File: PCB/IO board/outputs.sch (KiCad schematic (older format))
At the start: 20 parts

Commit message: Schematics Rev 1.0
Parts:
- gave numbers to parts that had none: 17
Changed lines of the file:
@@
 $Descr A4 11693 8268
 encoding utf-8
-Sheet 3 7
+Sheet 3 8
 Title ""
 Date ""
@@
 $EndDescr
 $Comp
-L MCP6004 U?
+L MCP6004 U301
 U 1 1 5ADC7D64
 P 2550 1700
-F 0 "U?" H 2550 1900 50  0000 L CNN
+F 0 "U301" H 2550 1900 50  0000 L CNN
 F 1 "TLV9064" H 2550 1500 50  0000 L CNN
 F 2 "" H 2500 1800 50  0001 C CNN
@@
 $EndComp
 $Comp
-L MCP6004 U?
+L MCP6004 U301
 U 2 1 5ADC7E6B
 P 2550 2600
-F 0 "U?" H 2550 2800 50  0000 L CNN
+F 0 "U301" H 2550 2800 50  0000 L CNN
 F 1 "TLV9064" H 2550 2400 50  0000 L CNN
 F 2 "" H 2500 2700 50  0001 C CNN
@@
 $EndComp
 $Comp
-L MCP6004 U?
+L MCP6004 U301
 U 3 1 5ADC7FEE
 P 2250 5000
-F 0 "U?" H 2250 5200 50  0000 L CNN
+F 0 "U301" H 2250 5200 50  0000 L CNN
 F 1 "TLV9064" H 2250 4800 50  0000 L CNN
 F 2 "" H 2200 5100 50  0001 C CNN
@@
 $EndComp
 $Comp
-L MCP6004 U?
+L MCP6004 U301
 U 4 1 5ADC8017
 P 2250 5900
-F 0 "U?" H 2250 6100 50  0000 L CNN
+F 0 "U301" H 2250 6100 50  0000 L CNN
 F 1 "TLV9064" H 2250 5700 50  0000 L CNN
 F 2 "" H 2200 6000 50  0001 C CNN
@@
 $EndComp
 $Comp
-L R R?
+L R R301
 U 1 1 5ADC8278
 P 1675 1600
-F 0 "R?" V 1755 1600 50  0000 C CNN
+F 0 "R301" V 1755 1600 50  0000 C CNN
 F 1 "51R" V 1675 1600 50  0000 C CNN
 F 2 "" V 1605 1600 50  0001 C CNN
@@
 $EndComp
 $Comp
-L C_Small C?
+L C_Small C302
 U 1 1 5ADC8327
 P 1925 2150
-F 0 "C?" H 1935 2220 50  0000 L CNN
+F 0 "C302" H 1935 2220 50  0000 L CNN
 F 1 "68nF" H 1935 2070 50  0000 L CNN
 F 2 "" H 1925 2150 50  0001 C CNN
@@
 $EndComp
 $Comp
-L GND #PWR?
+L GND #PWR016
 U 1 1 5ADC8546
 P 2400 2000
-F 0 "#PWR?" H 2400 1750 50  0001 C CNN
+F 0 "#PWR016" H 2400 1750 50  0001 C CNN
 F 1 "GND" H 2400 1850 50  0000 C CNN
 F 2 "" H 2400 2000 50  0001 C CNN
@@
 	2150 1800 2250 1800
 $Comp
-L GND #PWR?
+L GND #PWR017
 U 1 1 5ADC86E7
 P 2400 2300
-F 0 "#PWR?" H 2400 2050 50  0001 C CNN
+F 0 "#PWR017" H 2400 2050 50  0001 C CNN
 F 1 "GND" H 2400 2150 50  0000 C CNN
 F 2 "" H 2400 2300 50  0001 C CNN
@@
 	1825 2700 2250 2700
 $Comp
-L R R?
+L R R302
 U 1 1 5ADC8ADD
 P 1675 2700
-F 0 "R?" V 1755 2700 50  0000 C CNN
+F 0 "R302" V 1755 2700 50  0000 C CNN
 F 1 "51R" V 1675 2700 50  0000 C CNN
 F 2 "" V 1605 2700 50  0001 C CNN
@@
 	2450 2900 2450 3100
 $Comp
-L C_Small C?
+L C_Small C303
 U 1 1 5ADC9661
 P 3500 2600
-F 0 "C?" V 3550 2675 50  0000 L CNN
+F 0 "C303" V 3550 2675 50  0000 L CNN
 F 1 "10uF 100V" V 3550 2150 50  0000 L CNN
 F 2 "" H 3500 2600 50  0001 C CNN
@@
 $EndComp
 $Comp
-L D_Schottky_x2_ACom_KKA D?
+L D_Schottky_x2_ACom_KKA D301
 U 1 1 5ADC9B8C
 P 3125 2150
-F 0 "D?" V 3250 2000 50  0000 C CNN
+F 0 "D301" V 3250 2000 50  0000 C CNN
 F 1 "MMBZ5V6ALT1G" V 3025 1750 50  0000 C CNN
 F 2 "" H 3125 2150 50  0001 C CNN
@@
 Connection ~ 2950 2600
 $Comp
-L C_Small C?
+L C_Small C301
 U 1 1 5ADCA264
 P 3500 1700
-F 0 "C?" V 3550 1775 50  0000 L CNN
+F 0 "C301" V 3550 1775 50  0000 L CNN
 F 1 "10uF 100V" V 3550 1250 50  0000 L CNN
 F 2 "" H 3500 1700 50  0001 C CNN
@@
 $EndComp
 $Comp
-L Audio-Jack-3 J?
+L Audio-Jack-3 J301
 U 1 1 5ADCA5E0
 P 4300 2100
-F 0 "J?" H 4375 2025 50  0000 C CNN
+F 0 "J301" H 4375 2025 50  0000 C CNN
 F 1 "Audio-Jack-3" H 4150 2275 50  0000 C CNN
 F 2 "" H 4550 2200 50  0001 C CNN
@@
 	4500 1900 4600 1900
 $Comp
-L GND #PWR?
+L GND #PWR018
 U 1 1 5ADCB98E
 P 2100 5300
-F 0 "#PWR?" H 2100 5050 50  0001 C CNN
+F 0 "#PWR018" H 2100 5050 50  0001 C CNN
 F 1 "GND" H 2100 5150 50  0000 C CNN
 F 2 "" H 2100 5300 50  0001 C CNN
@@
 $EndComp
 $Comp
-L GND #PWR?
+L GND #PWR019
 U 1 1 5ADCB9D7
 P 2100 5600
-F 0 "#PWR?" H 2100 5350 50  0001 C CNN
+F 0 "#PWR019" H 2100 5350 50  0001 C CNN
 F 1 "GND" H 2100 5450 50  0000 C CNN
 F 2 "" H 2100 5600 50  0001 C CNN
@@
 	2150 4600 2150 4700
 $Comp
-L C_Small C?
+L C_Small C304
 U 1 1 5ADCC56F
 P 2450 3200
-F 0 "C?" H 2460 3270 50  0000 L CNN
+F 0 "C304" H 2460 3270 50  0000 L CNN
 F 1 "100nF" H 2460 3120 50  0000 L CNN
 F 2 "" H 2450 3200 50  0001 C CNN
@@
 Connection ~ 2450 3000
 $Comp
-L GND #PWR?
+L GND #PWR020
 U 1 1 5ADCC68B
 P 2450 3400
-F 0 "#PWR?" H 2450 3150 50  0001 C CNN
+F 0 "#PWR020" H 2450 3150 50  0001 C CNN
 F 1 "GND" H 2450 3250 50  0000 C CNN
 F 2 "" H 2450 3400 50  0001 C CNN
@@
 	2450 3300 2450 3400
 $Comp
-L C_Small C?
+L C_Small C306
 U 1 1 5ADCD4D6
 P 1625 5100
-F 0 "C?" H 1635 5170 50  0000 L CNN
+F 0 "C306" H 1635 5170 50  0000 L CNN
 F 1 "68nF" H 1635 5020 50  0000 L CNN
 F 2 "" H 1625 5100 50  0001 C CNN
@@
 	1525 4900 1950 4900
 $Comp
-L C_Small C?
+L C_Small C307
 U 1 1 5ADCD905
 P 1625 5800
-F 0 "C?" H 1635 5870 50  0000 L CNN
+F 0 "C307" H 1635 5870 50  0000 L CNN
 F 1 "68nF" H 1635 5720 50  0000 L CNN
 F 2 "" H 1625 5800 50  0001 C CNN
@@
 	1625 6000 1625 5900
 $Comp
-L GND #PWR?
+L GND #PWR021
 U 1 1 5ADCDA87
 P 1625 5250
-F 0 "#PWR?" H 1625 5000 50  0001 C CNN
+F 0 "#PWR021" H 1625 5000 50  0001 C CNN
 F 1 "GND" H 1625 5100 50  0000 C CNN
 F 2 "" H 1625 5250 50  0001 C CNN
@@
 $EndComp
 $Comp
-L GND #PWR?
+L GND #PWR022
 U 1 1 5ADCDAC2
 P 1625 5650
-F 0 "#PWR?" H 1625 5400 50  0001 C CNN
+F 0 "#PWR022" H 1625 5400 50  0001 C CNN
 F 1 "GND" H 1625 5500 50  0000 C CNN
 F 2 "" H 1625 5650 50  0001 C CNN
@@
 	1625 5700 1625 5650
 $Comp
-L R R?
+L R R303
 U 1 1 5ADCDD04
 P 1375 4900
-F 0 "R?" V 1455 4900 50  0000 C CNN
+F 0 "R303" V 1455 4900 50  0000 C CNN
 F 1 "100R" V 1375 4900 50  0000 C CNN
 F 2 "" V 1305 4900 50  0001 C CNN
@@
 $EndComp
 $Comp
-L R R?
+L R R304
 U 1 1 5ADCDFDD
 P 1375 6000
-F 0 "R?" V 1455 6000 50  0000 C CNN
+F 0 "R304" V 1455 6000 50  0000 C CNN
 F 1 "100R" V 1375 6000 50  0000 C CNN
 F 2 "" V 1305 6000 50  0001 C CNN
@@
 	1125 4900 1225 4900
 $Comp
-L D_Schottky_x2_ACom_KKA D?
+L D_Schottky_x2_ACom_KKA D302
 U 1 1 5ADCF378
 P 2850 5450
-F 0 "D?" V 2975 5300 50  0000 C CNN
+F 0 "D302" V 2975 5300 50  0000 C CNN
 F 1 "MMBZ5V6ALT1G" V 2750 5050 50  0000 C CNN
 F 2 "" H 2850 5450 50  0001 C CNN
@@
 Connection ~ 2650 5900
 $Comp
-L GND #PWR?
+L GND #PWR023
 U 1 1 5ADCF790
 P 3150 5450
-F 0 "#PWR?" H 3150 5200 50  0001 C CNN
+F 0 "#PWR023" H 3150 5200 50  0001 C CNN
 F 1 "GND" V 3200 5275 50  0000 C CNN
 F 2 "" H 3150 5450 50  0001 C CNN
@@
 	3050 5450 3150 5450
 $Comp
-L C_Small C?
+L C_Small C305
 U 1 1 5ADCF9BE
 P 3050 5000
-F 0 "C?" V 3100 5075 50  0000 L CNN
+F 0 "C305" V 3100 5075 50  0000 L CNN
 F 1 "10uF 10V" V 3100 4550 50  0000 L CNN
 F 2 "" H 3050 5000 50  0001 C CNN
@@
 $EndComp
 $Comp
-L C_Small C?
+L C_Small C308
 U 1 1 5ADCFBDE
 P 3050 5900
-F 0 "C?" V 3100 5975 50  0000 L CNN
+F 0 "C308" V 3100 5975 50  0000 L CNN
 F 1 "10uF 10V" V 3100 5450 50  0000 L CNN
 F 2 "" H 3050 5900 50  0001 C CNN
@@
 Connection ~ 2850 5000
 $Comp
-L 3.5mm_TRS_2SW X?
+L 3.5mm_TRS_2SW X301
 U 1 1 5ADD0316
 P 4175 5450
-F 0 "X?" H 4175 5800 60  0000 C CNN
+F 0 "X301" H 4175 5800 60  0000 C CNN
 F 1 "3.5mm_TRS_2SW" H 4575 5100 60  0000 C CNN
 F 2 "" H 3975 5450 60  0001 C CNN

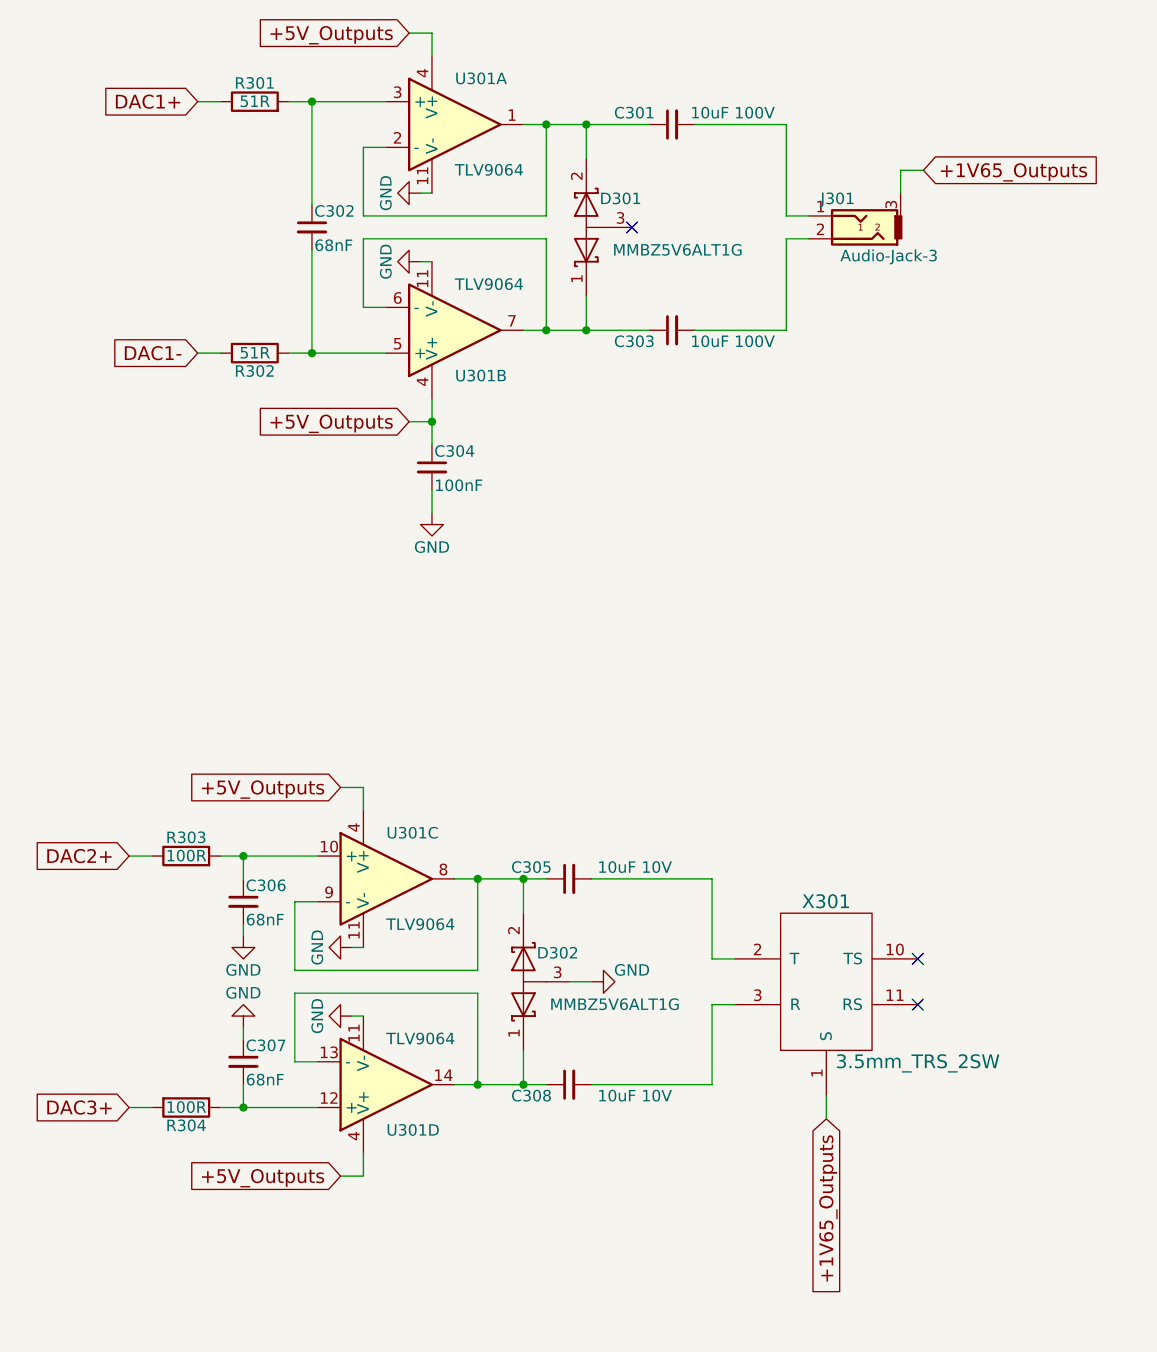
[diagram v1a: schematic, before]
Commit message: Component Placement - No pul-up
ALmost finished component placement expect for pull ups and low pass
filters for switches etc
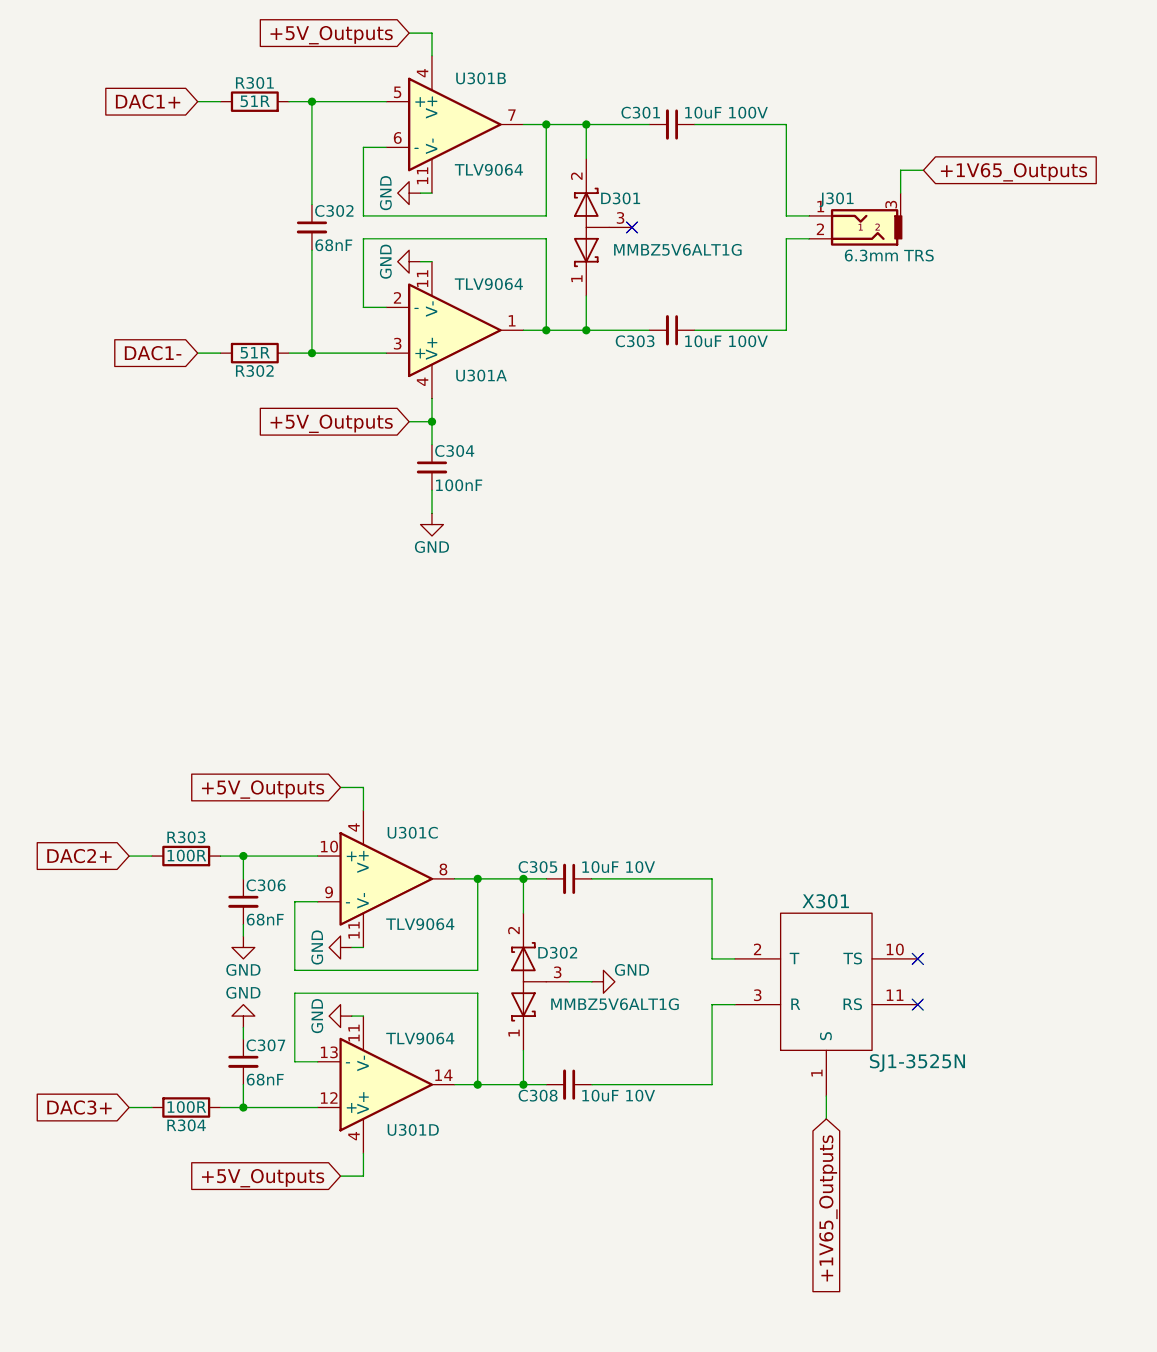
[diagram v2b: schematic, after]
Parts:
- C301, C303: footprint (none) -> Capacitors_THT:CP_Radial_D8.0mm_P3.50mm
- C302, C306, C307: footprint (none) -> Capacitors_THT:C_Rect_L7.5mm_W6.5mm_P5.00mm
- C304: footprint (none) -> Capacitors_SMD:C_0603
- C305, C308: footprint (none) -> Capacitors_SMD:CP_Elec_4x5.3
- D301, D302: footprint (none) -> TO_SOT_Packages_SMD:SOT-23
- J301: value Audio-Jack-3 -> 6.3mm TRS; footprint (none) -> Audio Connectors:NMJ6HFD2-NW
- R301, R302, R303, R304: footprint (none) -> Resistors_SMD:R_0603
- U301: footprint (none) -> Housings_SSOP:TSSOP-14_4.4x5mm_Pitch0.65mm
- X301: value 3.5mm_TRS_2SW -> SJ1-3525N; footprint (none) -> Audio Connectors:SJ1-352xN
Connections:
- net at U301.1, U301.2 (-): now also C303.2, D301.1 (K); no longer C301.1, D301.2 (K)
- net at C302.1, R301.2: now also U301.5 (+); no longer U301.3 (+)
- net at C302.2, R302.1: now also U301.3 (+); no longer U301.5 (+)
- net at U301.6 (-), U301.7: now also C301.2, D301.2 (K); no longer C303.1, D301.1 (K)
- net at D302.2 (K), U301.8, U301.9 (-): now also C305.2; no longer C305.1
- net at D302.1 (K), U301.13 (-), U301.14: now also C308.2; no longer C308.1
- net at J301.2: now also C303.1; no longer C303.2
- net at J301.1: now also C301.1; no longer C301.2
- net at X301.2 (T): now also C305.1; no longer C305.2
- net at X301.3 (R): now also C308.1; no longer C308.2
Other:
- moved on the sheet: U301A, U301B
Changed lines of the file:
@@
 L MCP6004 U301
 U 1 1 5ADC7D64
+P 2550 2600
+F 0 "U301" H 2550 2800 50  0000 L CNN
+F 1 "TLV9064" H 2550 2400 50  0000 L CNN
+F 2 "Housings_SSOP:TSSOP-14_4.4x5mm_Pitch0.65mm" H 2500 2700 50  0001 C CNN
+F 3 "" H 2600 2800 50  0001 C CNN
+	1    2550 2600
+	1    0    0    1
+$EndComp
+$Comp
+L MCP6004 U301
+U 2 1 5ADC7E6B
 P 2550 1700
 F 0 "U301" H 2550 1900 50  0000 L CNN
 F 1 "TLV9064" H 2550 1500 50  0000 L CNN
-F 2 "" H 2500 1800 50  0001 C CNN
+F 2 "Housings_SSOP:TSSOP-14_4.4x5mm_Pitch0.65mm" H 2500 1800 50  0001 C CNN
 F 3 "" H 2600 1900 50  0001 C CNN
-	1    2550 1700
-	1    0    0    -1
-$EndComp
-$Comp
-L MCP6004 U301
-U 2 1 5ADC7E6B
-P 2550 2600
-F 0 "U301" H 2550 2800 50  0000 L CNN
-F 1 "TLV9064" H 2550 2400 50  0000 L CNN
-F 2 "" H 2500 2700 50  0001 C CNN
-F 3 "" H 2600 2800 50  0001 C CNN
-	2    2550 2600
-	1    0    0    1
+	2    2550 1700
+	1    0    0    -1
 $EndComp
 $Comp
@@
 F 0 "U301" H 2250 5200 50  0000 L CNN
 F 1 "TLV9064" H 2250 4800 50  0000 L CNN
-F 2 "" H 2200 5100 50  0001 C CNN
+F 2 "Housings_SSOP:TSSOP-14_4.4x5mm_Pitch0.65mm" H 2200 5100 50  0001 C CNN
 F 3 "" H 2300 5200 50  0001 C CNN
 	3    2250 5000
@@
 F 0 "U301" H 2250 6100 50  0000 L CNN
 F 1 "TLV9064" H 2250 5700 50  0000 L CNN
-F 2 "" H 2200 6000 50  0001 C CNN
+F 2 "Housings_SSOP:TSSOP-14_4.4x5mm_Pitch0.65mm" H 2200 6000 50  0001 C CNN
 F 3 "" H 2300 6100 50  0001 C CNN
 	4    2250 5900
@@
 F 0 "R301" V 1755 1600 50  0000 C CNN
 F 1 "51R" V 1675 1600 50  0000 C CNN
-F 2 "" V 1605 1600 50  0001 C CNN
+F 2 "Resistors_SMD:R_0603" V 1605 1600 50  0001 C CNN
 F 3 "" H 1675 1600 50  0001 C CNN
 	1    1675 1600
@@
 F 0 "C302" H 1935 2220 50  0000 L CNN
 F 1 "68nF" H 1935 2070 50  0000 L CNN
-F 2 "" H 1925 2150 50  0001 C CNN
+F 2 "Capacitors_THT:C_Rect_L7.5mm_W6.5mm_P5.00mm" H 1925 2150 50  0001 C CNN
 F 3 "" H 1925 2150 50  0001 C CNN
 	1    1925 2150
@@
 F 0 "R302" V 1755 2700 50  0000 C CNN
 F 1 "51R" V 1675 2700 50  0000 C CNN
-F 2 "" V 1605 2700 50  0001 C CNN
+F 2 "Resistors_SMD:R_0603" V 1605 2700 50  0001 C CNN
 F 3 "" H 1675 2700 50  0001 C CNN
 	1    1675 2700
@@
 U 1 1 5ADC9661
 P 3500 2600
-F 0 "C303" V 3550 2675 50  0000 L CNN
-F 1 "10uF 100V" V 3550 2150 50  0000 L CNN
-F 2 "" H 3500 2600 50  0001 C CNN
+F 0 "C303" V 3550 2350 50  0000 L CNN
+F 1 "10uF 100V" V 3550 2650 50  0000 L CNN
+F 2 "Capacitors_THT:CP_Radial_D8.0mm_P3.50mm" H 3500 2600 50  0001 C CNN
 F 3 "" H 3500 2600 50  0001 C CNN
 	1    3500 2600
-	0    -1   1    0
+	0    1    1    0
 $EndComp
 $Comp
@@
 F 0 "D301" V 3250 2000 50  0000 C CNN
 F 1 "MMBZ5V6ALT1G" V 3025 1750 50  0000 C CNN
-F 2 "" H 3125 2150 50  0001 C CNN
+F 2 "TO_SOT_Packages_SMD:SOT-23" H 3125 2150 50  0001 C CNN
 F 3 "" H 3125 2150 50  0001 C CNN
 	1    3125 2150
@@
 U 1 1 5ADCA264
 P 3500 1700
-F 0 "C301" V 3550 1775 50  0000 L CNN
-F 1 "10uF 100V" V 3550 1250 50  0000 L CNN
-F 2 "" H 3500 1700 50  0001 C CNN
+F 0 "C301" V 3550 1475 50  0000 L CNN
+F 1 "10uF 100V" V 3550 1750 50  0000 L CNN
+F 2 "Capacitors_THT:CP_Radial_D8.0mm_P3.50mm" H 3500 1700 50  0001 C CNN
 F 3 "" H 3500 1700 50  0001 C CNN
 	1    3500 1700
-	0    -1   -1   0
-$EndComp
-$Comp
-L Audio-Jack-3 J301
-U 1 1 5ADCA5E0
-P 4300 2100
-F 0 "J301" H 4375 2025 50  0000 C CNN
-F 1 "Audio-Jack-3" H 4150 2275 50  0000 C CNN
-F 2 "" H 4550 2200 50  0001 C CNN
-F 3 "" H 4550 2200 50  0001 C CNN
-	1    4300 2100
-	-1   0    0    1
+	0    1    -1   0
 $EndComp
 Wire Wire Line
@@
 F 0 "C304" H 2460 3270 50  0000 L CNN
 F 1 "100nF" H 2460 3120 50  0000 L CNN
-F 2 "" H 2450 3200 50  0001 C CNN
+F 2 "Capacitors_SMD:C_0603" H 2450 3200 50  0001 C CNN
 F 3 "" H 2450 3200 50  0001 C CNN
 	1    2450 3200
@@
 F 0 "C306" H 1635 5170 50  0000 L CNN
 F 1 "68nF" H 1635 5020 50  0000 L CNN
-F 2 "" H 1625 5100 50  0001 C CNN
+F 2 "Capacitors_THT:C_Rect_L7.5mm_W6.5mm_P5.00mm" H 1625 5100 50  0001 C CNN
 F 3 "" H 1625 5100 50  0001 C CNN
 	1    1625 5100
@@
 F 0 "C307" H 1635 5870 50  0000 L CNN
 F 1 "68nF" H 1635 5720 50  0000 L CNN
-F 2 "" H 1625 5800 50  0001 C CNN
+F 2 "Capacitors_THT:C_Rect_L7.5mm_W6.5mm_P5.00mm" H 1625 5800 50  0001 C CNN
 F 3 "" H 1625 5800 50  0001 C CNN
 	1    1625 5800
@@
 F 0 "R303" V 1455 4900 50  0000 C CNN
 F 1 "100R" V 1375 4900 50  0000 C CNN
-F 2 "" V 1305 4900 50  0001 C CNN
+F 2 "Resistors_SMD:R_0603" V 1305 4900 50  0001 C CNN
 F 3 "" H 1375 4900 50  0001 C CNN
 	1    1375 4900
@@
 F 0 "R304" V 1455 6000 50  0000 C CNN
 F 1 "100R" V 1375 6000 50  0000 C CNN
-F 2 "" V 1305 6000 50  0001 C CNN
+F 2 "Resistors_SMD:R_0603" V 1305 6000 50  0001 C CNN
 F 3 "" H 1375 6000 50  0001 C CNN
 	1    1375 6000
@@
 F 0 "D302" V 2975 5300 50  0000 C CNN
 F 1 "MMBZ5V6ALT1G" V 2750 5050 50  0000 C CNN
-F 2 "" H 2850 5450 50  0001 C CNN
+F 2 "TO_SOT_Packages_SMD:SOT-23" H 2850 5450 50  0001 C CNN
 F 3 "" H 2850 5450 50  0001 C CNN
 	1    2850 5450
@@
 U 1 1 5ADCF9BE
 P 3050 5000
-F 0 "C305" V 3100 5075 50  0000 L CNN
-F 1 "10uF 10V" V 3100 4550 50  0000 L CNN
-F 2 "" H 3050 5000 50  0001 C CNN
+F 0 "C305" V 3100 4775 50  0000 L CNN
+F 1 "10uF 10V" V 3100 5050 50  0000 L CNN
+F 2 "Capacitors_SMD:CP_Elec_4x5.3" H 3050 5000 50  0001 C CNN
 F 3 "" H 3050 5000 50  0001 C CNN
 	1    3050 5000
-	0    -1   -1   0
+	0    1    -1   0
 $EndComp
 $Comp
@@
 U 1 1 5ADCFBDE
 P 3050 5900
-F 0 "C308" V 3100 5975 50  0000 L CNN
-F 1 "10uF 10V" V 3100 5450 50  0000 L CNN
-F 2 "" H 3050 5900 50  0001 C CNN
+F 0 "C308" V 3100 5675 50  0000 L CNN
+F 1 "10uF 10V" V 3100 5950 50  0000 L CNN
+F 2 "Capacitors_SMD:CP_Elec_4x5.3" H 3050 5900 50  0001 C CNN
 F 3 "" H 3050 5900 50  0001 C CNN
 	1    3050 5900
-	0    -1   1    0
+	0    1    1    0
 $EndComp
 Connection ~ 2850 5900
@@
 P 4175 5450
 F 0 "X301" H 4175 5800 60  0000 C CNN
-F 1 "3.5mm_TRS_2SW" H 4575 5100 60  0000 C CNN
-F 2 "" H 3975 5450 60  0001 C CNN
+F 1 "SJ1-3525N" H 4575 5100 60  0000 C CNN
+F 2 "Audio Connectors:SJ1-352xN" H 3975 5450 60  0001 C CNN
 F 3 "" H 3975 5450 60  0001 C CNN
 	1    4175 5450
@@
 NoConn ~ 4575 5350
 NoConn ~ 4575 5550
+$Comp
+L Audio-Jack-3 J301
+U 1 1 5ADCA5E0
+P 4300 2100
+F 0 "J301" H 4375 2025 50  0000 C CNN
+F 1 "6.3mm TRS" H 4150 2275 50  0000 C CNN
+F 2 "Audio Connectors:NMJ6HFD2-NW" H 4550 2200 50  0001 C CNN
+F 3 "" H 4550 2200 50  0001 C CNN
+	1    4300 2100
+	-1   0    0    1
+$EndComp
 $EndSCHEMATC
